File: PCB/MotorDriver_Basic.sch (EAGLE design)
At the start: 15 parts, among them IC1 MPU6050, U1 DRV8835

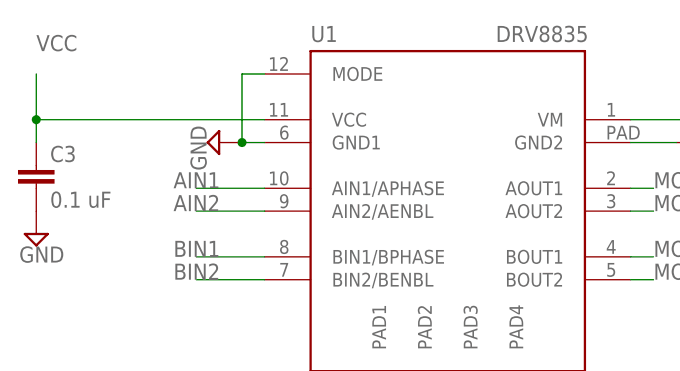
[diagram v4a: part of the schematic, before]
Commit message: Fixed the fucking asshole's mistake where the fuck did we get that fucking foot print fuck fuck fuck fuck fuck
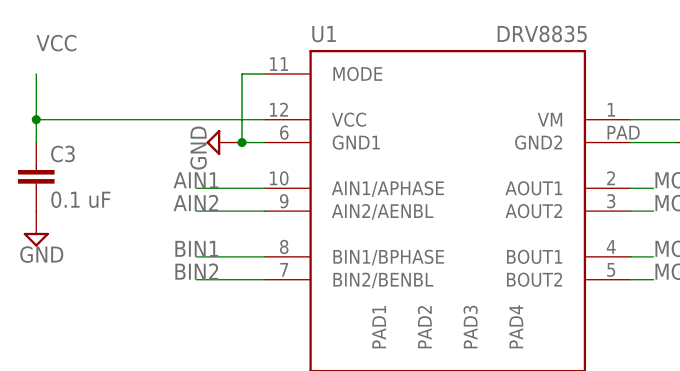
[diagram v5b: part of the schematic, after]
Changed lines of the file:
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@@
 <?xml version="1.0" encoding="utf-8"?>
 <!DOCTYPE eagle SYSTEM "eagle.dtd">
-<eagle version="9.2.2">
+<eagle version="9.3.2">
 <drawing>
 <settings>
@@
 <grid distance="0.1" unitdist="inch" unit="inch" style="lines" multiple="1" display="no" altdistance="0.01" altunitdist="inch" altunit="inch"/>
 <layers>
-<layer number="1" name="Top" color="4" fill="1" visible="no" active="no"/>
-<layer number="2" name="Route2" color="1" fill="3" visible="no" active="no"/>
-<layer number="3" name="Route3" color="4" fill="3" visible="no" active="no"/>
-<layer number="4" name="Route4" color="1" fill="4" visible="no" active="no"/>
-<layer number="5" name="Route5" color="4" fill="4" visible="no" active="no"/>
-<layer number="6" name="Route6" color="1" fill="8" visible="no" active="no"/>
-<layer number="7" name="Route7" color="4" fill="8" visible="no" active="no"/>
-<layer number="8" name="Route8" color="1" fill="2" visible="no" active="no"/>
-<layer number="9" name="Route9" color="4" fill="2" visible="no" active="no"/>
-<layer number="10" name="Route10" color="1" fill="7" visible="no" active="no"/>
-<layer number="11" name="Route11" color="4" fill="7" visible="no" active="no"/>
-<layer number="12" name="Route12" color="1" fill="5" visible="no" active="no"/>
-<layer number="13" name="Route13" color="4" fill="5" visible="no" active="no"/>
-<layer number="14" name="Route14" color="1" fill="6" visible="no" active="no"/>
-<layer number="15" name="Route15" color="4" fill="6" visible="no" active="no"/>
-<layer number="16" name="Bottom" color="1" fill="1" visible="no" active="no"/>
-<layer number="17" name="Pads" color="2" fill="1" visible="no" active="no"/>
-<layer number="18" name="Vias" color="2" fill="1" visible="no" active="no"/>
-<layer number="19" name="Unrouted" color="6" fill="1" visible="no" active="no"/>
-<layer number="20" name="Dimension" color="24" fill="1" visible="no" active="no"/>
-<layer number="21" name="tPlace" color="7" fill="1" visible="no" active="no"/>
-<layer number="22" name="bPlace" color="7" fill="1" visible="no" active="no"/>
-<layer number="23" name="tOrigins" color="15" fill="1" visible="no" active="no"/>
-<layer number="24" name="bOrigins" color="15" fill="1" visible="no" active="no"/>
-<layer number="25" name="tNames" color="7" fill="1" visible="no" active="no"/>
-<layer number="26" name="bNames" color="7" fill="1" visible="no" active="no"/>
-<layer number="27" name="tValues" color="7" fill="1" visible="no" active="no"/>
-<layer number="28" name="bValues" color="7" fill="1" visible="no" active="no"/>
+<layer number="1" name="Top" color="4" fill="1" visible="yes" active="no"/>
+<layer number="2" name="Route2" color="1" fill="3" visible="yes" active="no"/>
+<layer number="3" name="Route3" color="4" fill="3" visible="yes" active="no"/>
+<layer number="4" name="Route4" color="1" fill="4" visible="yes" active="no"/>
+<layer number="5" name="Route5" color="4" fill="4" visible="yes" active="no"/>
+<layer number="6" name="Route6" color="1" fill="8" visible="yes" active="no"/>
+<layer number="7" name="Route7" color="4" fill="8" visible="yes" active="no"/>
+<layer number="8" name="Route8" color="1" fill="2" visible="yes" active="no"/>
+<layer number="9" name="Route9" color="4" fill="2" visible="yes" active="no"/>
+<layer number="10" name="Route10" color="1" fill="7" visible="yes" active="no"/>
+<layer number="11" name="Route11" color="4" fill="7" visible="yes" active="no"/>
+<layer number="12" name="Route12" color="1" fill="5" visible="yes" active="no"/>
+<layer number="13" name="Route13" color="4" fill="5" visible="yes" active="no"/>
+<layer number="14" name="Route14" color="1" fill="6" visible="yes" active="no"/>
+<layer number="15" name="Route15" color="4" fill="6" visible="yes" active="no"/>
+<layer number="16" name="Bottom" color="1" fill="1" visible="yes" active="no"/>
+<layer number="17" name="Pads" color="2" fill="1" visible="yes" active="no"/>
+<layer number="18" name="Vias" color="2" fill="1" visible="yes" active="no"/>
+<layer number="19" name="Unrouted" color="6" fill="1" visible="yes" active="no"/>
+<layer number="20" name="Dimension" color="24" fill="1" visible="yes" active="no"/>
+<layer number="21" name="tPlace" color="7" fill="1" visible="yes" active="no"/>
+<layer number="22" name="bPlace" color="7" fill="1" visible="yes" active="no"/>
+<layer number="23" name="tOrigins" color="15" fill="1" visible="yes" active="no"/>
+<layer number="24" name="bOrigins" color="15" fill="1" visible="yes" active="no"/>
+<layer number="25" name="tNames" color="7" fill="1" visible="yes" active="no"/>
+<layer number="26" name="bNames" color="7" fill="1" visible="yes" active="no"/>
+<layer number="27" name="tValues" color="7" fill="1" visible="yes" active="no"/>
+<layer number="28" name="bValues" color="7" fill="1" visible="yes" active="no"/>
 <layer number="29" name="tStop" color="7" fill="3" visible="no" active="no"/>
 <layer number="30" name="bStop" color="7" fill="6" visible="no" active="no"/>
@@
 <layer number="35" name="tGlue" color="7" fill="4" visible="no" active="no"/>
 <layer number="36" name="bGlue" color="7" fill="5" visible="no" active="no"/>
-<layer number="37" name="tTest" color="7" fill="1" visible="no" active="no"/>
-<layer number="38" name="bTest" color="7" fill="1" visible="no" active="no"/>
+<layer number="37" name="tTest" color="7" fill="1" visible="yes" active="no"/>
+<layer number="38" name="bTest" color="7" fill="1" visible="yes" active="no"/>
 <layer number="39" name="tKeepout" color="4" fill="11" visible="no" active="no"/>
 <layer number="40" name="bKeepout" color="1" fill="11" visible="no" active="no"/>
@@
 <layer number="44" name="Drills" color="7" fill="1" visible="no" active="no"/>
 <layer number="45" name="Holes" color="7" fill="1" visible="no" active="no"/>
-<layer number="46" name="Milling" color="3" fill="1" visible="no" active="no"/>
-<layer number="47" name="Measures" color="7" fill="1" visible="no" active="no"/>
-<layer number="48" name="Document" color="7" fill="1" visible="no" active="no"/>
-<layer number="49" name="Reference" color="7" fill="1" visible="no" active="no"/>
-<layer number="50" name="dxf" color="7" fill="1" visible="no" active="no"/>
-<layer number="51" name="tDocu" color="7" fill="1" visible="no" active="no"/>
-<layer number="52" name="bDocu" color="7" fill="1" visible="no" active="no"/>
-<layer number="53" name="tGND_GNDA" color="7" fill="9" visible="no" active="no"/>
-<layer number="54" name="bGND_GNDA" color="1" fill="9" visible="no" active="no"/>
-<layer number="56" name="wert" color="7" fill="1" visible="no" active="no"/>
-<layer number="57" name="tCAD" color="7" fill="1" visible="no" active="no"/>
-<layer number="59" name="tCarbon" color="7" fill="1" visible="no" active="no"/>
-<layer number="60" name="bCarbon" color="7" fill="1" visible="no" active="no"/>
+<layer number="46" name="Milling" color="3" fill="1" visible="yes" active="no"/>
+<layer number="47" name="Measures" color="7" fill="1" visible="yes" active="no"/>
+<layer number="48" name="Document" color="7" fill="1" visible="yes" active="no"/>
+<layer number="49" name="Reference" color="7" fill="1" visible="yes" active="no"/>
+<layer number="50" name="dxf" color="7" fill="1" visible="yes" active="no"/>
+<layer number="51" name="tDocu" color="7" fill="1" visible="yes" active="no"/>
+<layer number="52" name="bDocu" color="7" fill="1" visible="yes" active="no"/>
+<layer number="53" name="tGND_GNDA" color="7" fill="9" visible="yes" active="no"/>
+<layer number="54" name="bGND_GNDA" color="1" fill="9" visible="yes" active="no"/>
+<layer number="56" name="wert" color="7" fill="1" visible="yes" active="no"/>
+<layer number="57" name="tCAD" color="7" fill="1" visible="yes" active="no"/>
+<layer number="59" name="tCarbon" color="7" fill="1" visible="yes" active="no"/>
+<layer number="60" name="bCarbon" color="7" fill="1" visible="yes" active="no"/>
 <layer number="88" name="SimResults" color="9" fill="1" visible="yes" active="yes"/>
 <layer number="89" name="SimProbes" color="9" fill="1" visible="yes" active="yes"/>
